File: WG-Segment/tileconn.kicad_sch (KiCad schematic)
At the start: 41 parts, among them J501 Conn_01x02, J502 Conn_01x02, J503 Conn_01x02, J504 Conn_01x02, J505 Conn_01x02, J506 Conn_01x02, J507 Conn_01x02, J508 Conn_01x02, J509 Conn_01x02, J510 Conn_01x02, J511 Conn_01x02, J512 Conn_01x02, J513 Conn_01x02, J514 Conn_01x02, J515 Conn_01x02, J516 Conn_01x02, J517 Conn_01x02, J518 Conn_01x02, J519 Conn_01x02, J520 Conn_01x02, J521 Conn_01x02, J522 Conn_01x02, J523 Conn_01x02, J524 Conn_01x02, J525 Conn_01x02, U501 SN74LV4051A, U502 SN74LV4051A, U503 SN74LV4051A, U504 SN74LV4051A

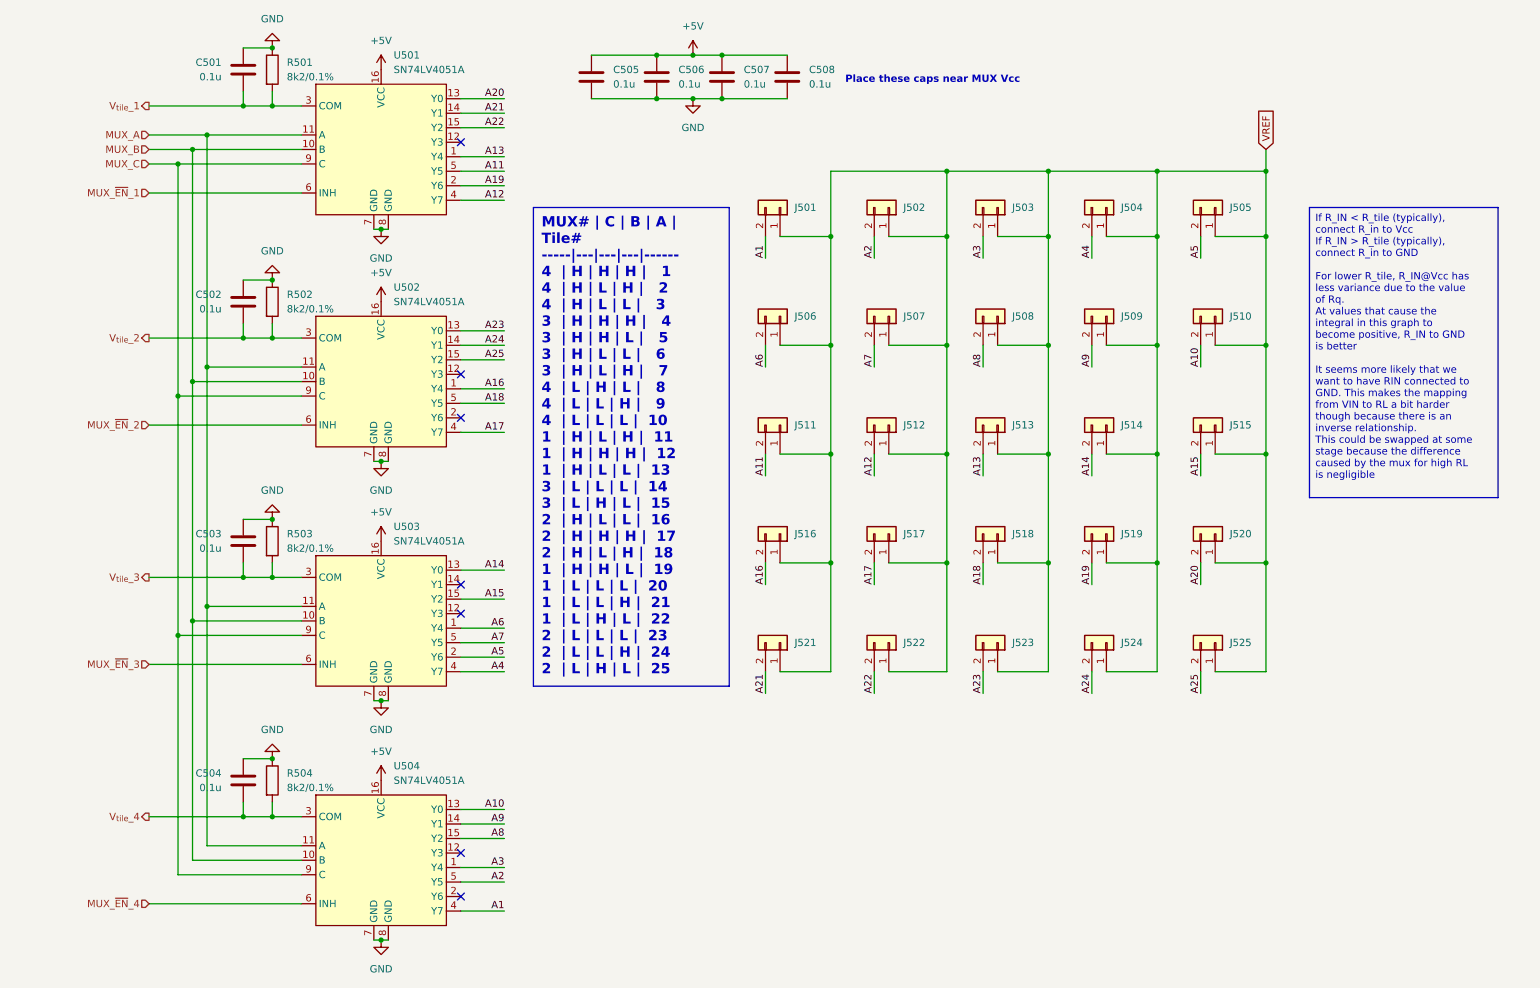
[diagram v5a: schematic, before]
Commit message: Updates for smoother JLCPCB ordering
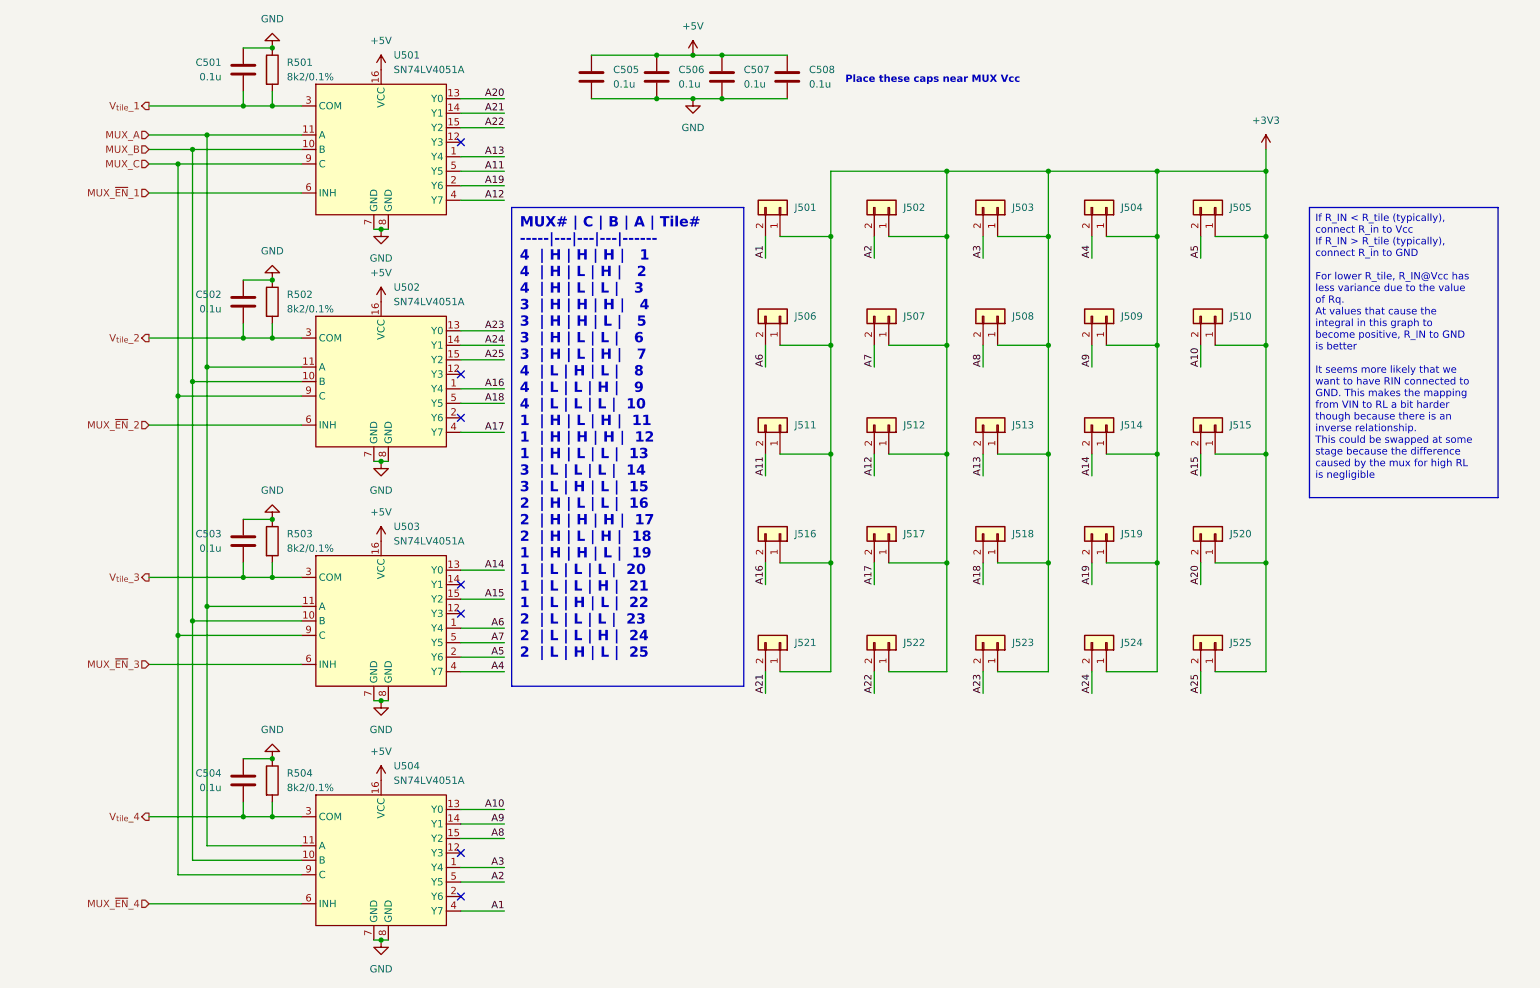
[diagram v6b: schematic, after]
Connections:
- net VREF renamed +3V3
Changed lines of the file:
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@@
   )
   (text_box "MUX# | C | B | A | Tile#\n-----|---|---|---|------\n  4  | H | H | H |   1\n  4  | H | L | H |   2\n  4  | H | L | L |   3\n  3  | H | H | H |   4\n  3  | H | H | L |   5\n  3  | H | L | L |   6\n  3  | H | L | H |   7\n  4  | L | H | L |   8\n  4  | L | L | H |   9\n  4  | L | L | L |  10\n  1  | H | L | H |  11\n  1  | H | H | H |  12\n  1  | H | L | L |  13\n  3  | L | L | L |  14\n  3  | L | H | L |  15\n  2  | H | L | L |  16\n  2  | H | H | H |  17\n  2  | H | L | H |  18\n  1  | H | H | L |  19\n  1  | L | L | L |  20\n  1  | L | L | H |  21\n  1  | L | H | L |  22\n  2  | L | L | L |  23\n  2  | L | L | H |  24\n  2  | L | H | L |  25"
-    (at 110.49 52.07 0) (size 34.29 83.82)
+    (at 106.68 52.07 0) (size 40.64 83.82)
     (stroke (width 0) (type default))
     (fill (type color) (color 255 229 191 1))
-    (effects (font (face "Ubuntu Mono") (size 1.8 1.8) (thickness 0.254) bold) (justify left top))
+    (effects (font (face "DejaVu Sans Mono") (size 1.8 1.8) (thickness 0.254) bold) (justify left top))
   )
   (text "Place these caps near MUX Vcc" (at 165.1 30.48 0)
@@
   (label "A21" (at 105.41 35.56 180) (fields_autoplaced)
     (effects (font (size 1.27 1.27)) (justify right bottom))
-  )
-  (global_label "VREF" (shape input) (at 238.76 41.91 90) (fields_autoplaced)
-    (effects (font (size 1.27 1.27)) (justify left))
-    (property "Intersheetrefs" "${INTERSHEET_REFS}" (at 238.76 34.3286 90)
-      (effects (font (size 1.27 1.27)) (justify left) hide)
-    )
   )
   (hierarchical_label "MUX_~{EN}_2" (shape input) (at 43.18 90.17 180) (fields_autoplaced)
@@
         )
       )
+    )
+  )
+  (symbol (lib_id "power:+3V3") (at 238.76 41.91 0) (unit 1)
+    (in_bom yes) (on_board yes) (dnp no) (fields_autoplaced)
+    (property "Reference" "#PWR0515" (at 238.76 45.72 0)
+      (effects (font (size 1.27 1.27)) hide)
+    )
+    (property "Value" "+3V3" (at 238.76 36.83 0)
+      (effects (font (size 1.27 1.27)))
+    )
+    (property "Footprint" "" (at 238.76 41.91 0)
+      (effects (font (size 1.27 1.27)) hide)
+    )
+    (property "Datasheet" "" (at 238.76 41.91 0)
+      (effects (font (size 1.27 1.27)) hide)
+    )
+    (pin "1")
+    (instances
+      (project "WG-Segment"
+        (path "/9a5339e6-f970-4986-a2cb-f70ab323b7e1/2b040784-7c57-4701-9a06-95f5fc63b367"
+          (reference "#PWR0515") (unit 1)
+        )
+      )

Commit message: Add LCSC part numbers
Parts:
- C501, C502, C503, C504, C505, C506, C507, C508: LCSC Part (none) -> C1525
- R501, R502, R503, R504: LCSC Part (none) -> C25924
- U501, U502, U503, U504: LCSC Part (none) -> C7793
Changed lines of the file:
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@@
+      (effects (font (size 1.27 1.27)) hide)
+    )
+    (property "LCSC Part" "C1525" (at 59.69 152.4 0)
       (effects (font (size 1.27 1.27)) hide)
     )
@@
     )
     (property "Desc" "CAP CER 0.1uF 10V 0402" (at 143.51 29.21 0)
+      (effects (font (size 1.27 1.27)) hide)
+    )
+    (property "LCSC Part" "C1525" (at 143.51 29.21 0)
       (effects (font (size 1.27 1.27)) hide)
     )
@@
       (effects (font (size 1.27 1.27)) hide)
     )
+    (property "LCSC Part" "C1525" (at 59.69 27.94 0)
+      (effects (font (size 1.27 1.27)) hide)
+    )
     (pin "1")
     (pin "2")
@@
       (effects (font (size 1.27 1.27)) hide)
     )
+    (property "LCSC Part" "C1525" (at 120.65 29.21 0)
+      (effects (font (size 1.27 1.27)) hide)
+    )
     (pin "1")
     (pin "2")
@@
     )
     (property "Desc" "CAP CER 0.1uF 10V 0402" (at 154.94 29.21 0)
+      (effects (font (size 1.27 1.27)) hide)
+    )
+    (property "LCSC Part" "C1525" (at 154.94 29.21 0)
       (effects (font (size 1.27 1.27)) hide)
     )
@@
       (effects (font (size 1.27 1.27)) hide)
     )
+    (property "LCSC Part" "C1525" (at 132.08 29.21 0)
+      (effects (font (size 1.27 1.27)) hide)
+    )
     (pin "1")
     (pin "2")
@@
       (effects (font (size 1.27 1.27)) hide)
     )
+    (property "LCSC Part" "C25924" (at 64.77 110.49 0)
+      (effects (font (size 1.27 1.27)) hide)
+    )
     (pin "2")
     (pin "1")
@@
     )
     (property "Desc" "" (at 83.82 105.41 0)
+      (effects (font (size 1.27 1.27)) hide)
+    )
+    (property "LCSC Part" "C7793" (at 83.82 105.41 0)
       (effects (font (size 1.27 1.27)) hide)
     )
@@
       (effects (font (size 1.27 1.27)) hide)
     )
+    (property "LCSC Part" "C25924" (at 64.77 152.4 0)
+      (effects (font (size 1.27 1.27)) hide)
+    )
     (pin "2")
     (pin "1")
@@
       (effects (font (size 1.27 1.27)) hide)
     )
+    (property "LCSC Part" "C1525" (at 59.69 110.49 0)
+      (effects (font (size 1.27 1.27)) hide)
+    )
     (pin "1")
     (pin "2")
@@
       (effects (font (size 1.27 1.27)) hide)
     )
+    (property "LCSC Part" "C25924" (at 64.77 27.94 0)
+      (effects (font (size 1.27 1.27)) hide)
+    )
     (pin "2")
     (pin "1")
@@
     )
     (property "Desc" "" (at 83.82 147.32 0)
+      (effects (font (size 1.27 1.27)) hide)
+    )
+    (property "LCSC Part" "C7793" (at 83.82 147.32 0)
       (effects (font (size 1.27 1.27)) hide)
     )
@@
       (effects (font (size 1.27 1.27)) hide)
     )
+    (property "LCSC Part" "C1525" (at 59.69 68.58 0)
+      (effects (font (size 1.27 1.27)) hide)
+    )
     (pin "1")
     (pin "2")
@@
     )
     (property "Desc" "" (at 83.82 63.5 0)
+      (effects (font (size 1.27 1.27)) hide)
+    )
+    (property "LCSC Part" "C7793" (at 83.82 63.5 0)
       (effects (font (size 1.27 1.27)) hide)
     )
@@
       (effects (font (size 1.27 1.27)) hide)
     )
+    (property "LCSC Part" "C25924" (at 64.77 68.58 0)
+      (effects (font (size 1.27 1.27)) hide)
+    )
     (pin "2")
     (pin "1")
@@
       (effects (font (size 1.27 1.27)) hide)
     )
+    (property "LCSC Part" "C7793" (at 83.82 22.86 0)
+      (effects (font (size 1.27 1.27)) hide)
+    )
